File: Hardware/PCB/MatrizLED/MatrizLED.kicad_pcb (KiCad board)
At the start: 2 copper layers, 85.7 x 95.3 mm, 23 parts, among them M1_L1 CONN_01X06, M1_R1 CONN_01X06, M2_L1 CONN_01X06, M2_R1 CONN_01X06, M3_L1 CONN_01X06, M3_R1 CONN_01X06, M4_L1 CONN_01X06, M4_R1 CONN_01X06

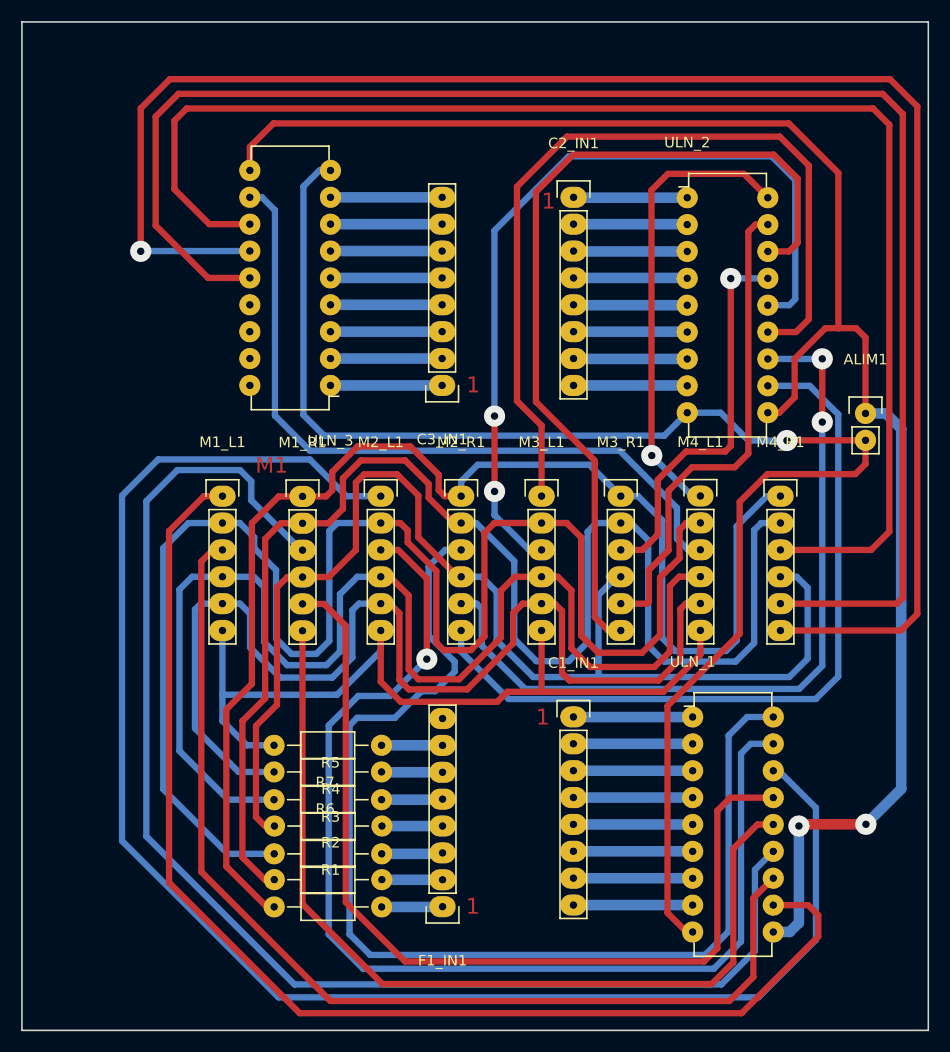
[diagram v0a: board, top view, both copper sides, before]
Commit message: Actualizada placa de matrices
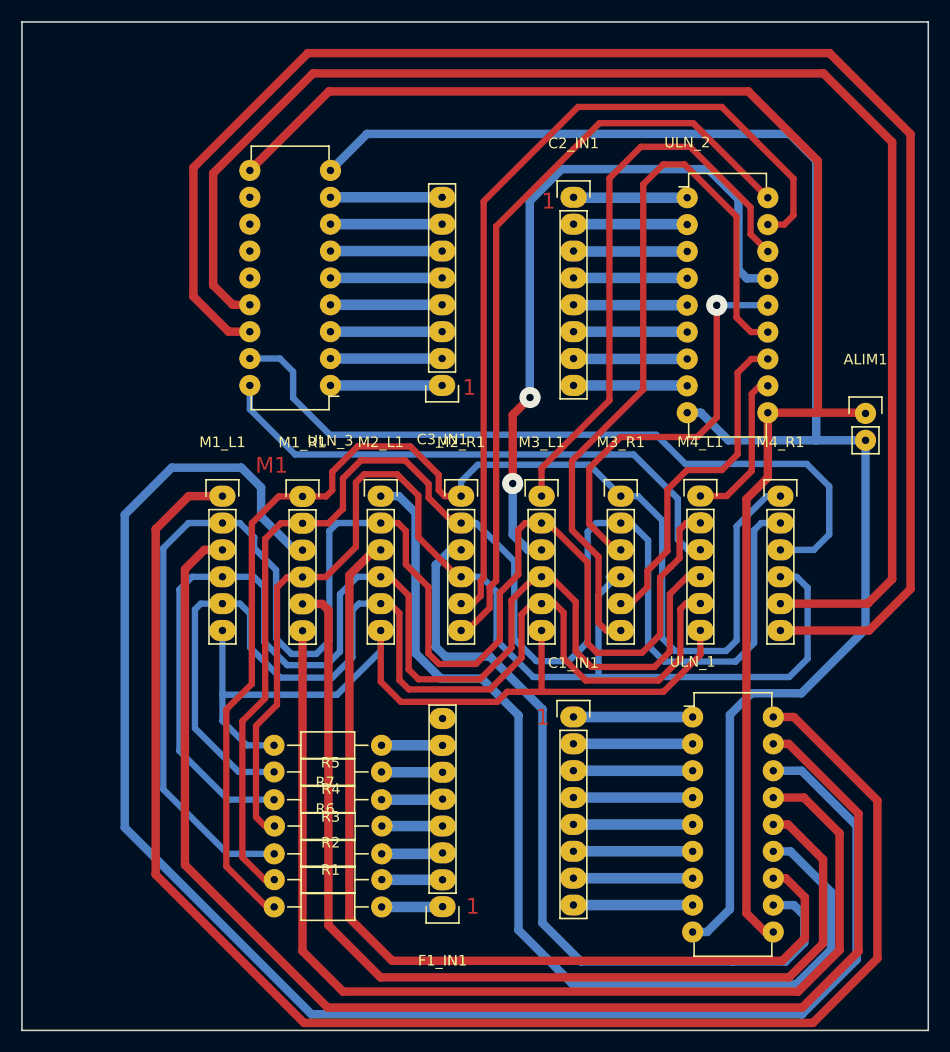
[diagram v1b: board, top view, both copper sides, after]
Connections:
- ULN_1 pad 11: Net-(M1_L1-Pad1) -> Net-(M2_R1-Pad3)
- ULN_1 pad 12: Net-(M1_L1-Pad3) -> Net-(M2_L1-Pad3)
- ULN_1 pad 13: Net-(M1_R1-Pad3) -> Net-(M2_L1-Pad1)
- ULN_1 pad 14: Net-(M1_R1-Pad6) -> Net-(M1_R1-Pad5)
- ULN_1 pad 15: Net-(M1_R1-Pad5) -> Net-(M1_R1-Pad6)
- ULN_1 pad 16: Net-(M2_L1-Pad1) -> Net-(M1_R1-Pad3)
- ULN_1 pad 17: Net-(M2_L1-Pad3) -> Net-(M1_L1-Pad3)
- ULN_1 pad 18: Net-(M2_R1-Pad3) -> Net-(M1_L1-Pad1)
- ULN_2 pad 11: Net-(M2_R1-Pad6) -> Net-(M4_L1-Pad1)
- ULN_2 pad 12: Net-(M2_R1-Pad5) -> Net-(M3_R1-Pad5)
- ULN_2 pad 13: Net-(M3_L1-Pad1) -> Net-(M3_R1-Pad6)
- ULN_2 pad 14: Net-(M3_L1-Pad3) -> Net-(M3_R1-Pad3)
- ULN_2 pad 15: Net-(M3_R1-Pad3) -> Net-(M3_L1-Pad3)
- ULN_2 pad 16: Net-(M3_R1-Pad6) -> Net-(M3_L1-Pad1)
- ULN_2 pad 17: Net-(M3_R1-Pad5) -> Net-(M2_R1-Pad5)
- ULN_2 pad 18: Net-(M4_L1-Pad1) -> Net-(M2_R1-Pad6)
- ULN_3 pad 11: Net-(M4_L1-Pad3) -> Net-(ULN_3-Pad11)
- ULN_3 pad 12: Net-(M4_R1-Pad3) -> Net-(ULN_3-Pad12)
- ULN_3 pad 13: Net-(M4_R1-Pad6) -> Net-(ULN_3-Pad13)
- ULN_3 pad 14: Net-(M4_R1-Pad5) -> Net-(ULN_3-Pad14)
- ULN_3 pad 15: Net-(ULN_3-Pad15) -> Net-(M4_R1-Pad5)
- ULN_3 pad 16: Net-(ULN_3-Pad16) -> Net-(M4_R1-Pad6)
- ULN_3 pad 17: Net-(ULN_3-Pad17) -> Net-(M4_R1-Pad3)
- ULN_3 pad 18: Net-(ULN_3-Pad18) -> Net-(M4_L1-Pad3)
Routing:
- net Net-(M4_R1-Pad3): track 133.1 -> 71.0 mm
- net Net-(M2_L1-Pad1): track 151.9 -> 95.2 mm
- net Net-(M2_R1-Pad3): track 107.5 -> 76.4 mm
- net Net-(M1_L1-Pad1): track 115.8 -> 144.8 mm
- net Net-(M1_R1-Pad3): track 126.6 -> 155.0 mm
- net Net-(M1_L1-Pad3): track 100.1 -> 128.4 mm
- net Net-(M4_L1-Pad1): track 43.9 -> 15.7 mm, vias 1 -> 0
- net Net-(M3_L1-Pad1): track 79.8 -> 54.5 mm
- net Net-(M2_L1-Pad3): track 110.1 -> 92.2 mm, vias 1 -> 0
- net Net-(M1_R1-Pad6): track 86.0 -> 102.9 mm
- net Net-(M4_L1-Pad3): track 69.5 -> 53.8 mm
- net VCC: track 158.7 -> 144.6 mm, vias 2 -> 0
- net Net-(M3_R1-Pad5): track 46.1 -> 33.3 mm
- net Net-(M4_R1-Pad5): track 151.1 -> 138.4 mm
- net Net-(M3_L1-Pad3): track 79.1 -> 68.6 mm
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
